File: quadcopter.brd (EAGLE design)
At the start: 127.2 x 127.2 mm, 77 parts, among them J1 AVR_SPI_PRG_6NS, J3 HEADER-0.1IN-2POS-FEMALE, J4 HEADER-0.1IN-2POS-FEMALE, J5 HEADER-0.1IN-2POS-FEMALE, J6 HEADER-0.1IN-2POS-FEMALE, J8 HEADER-0.1IN-2POS-FEMALE, SW1 PUSHBUTTON_SMD-VERTICAL, SW2 PUSHBUTTON_SMD-VERTICAL, U1 ATMEGA128RFA1

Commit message: fixed attenna
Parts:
- moved C2 0.13 mm to (-3.62, 23.8)
- moved C1 0.13 mm to (-3.37, 21.5)
- moved U$1 0.13 mm to (0.00, 29.7)
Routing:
- net GND: track 257.7 -> 246.4 mm, vias 8 -> 7

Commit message: changed caps, moving grounds
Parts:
- C18, C19, C20, C21: value 1uF -> 0.1uF
- moved C16 1.23 mm to (-24.1, -6.62), turned to 90 degrees
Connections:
- net BAT_GND: now also C16.2
- net GND: no longer C16.2
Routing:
- net GND: track 246.4 -> 251.7 mm
- net BAT_GND: track 143.7 -> 147.5 mm, vias 0 -> 1
- net V_BAT: track 85.6 -> 82.0 mm

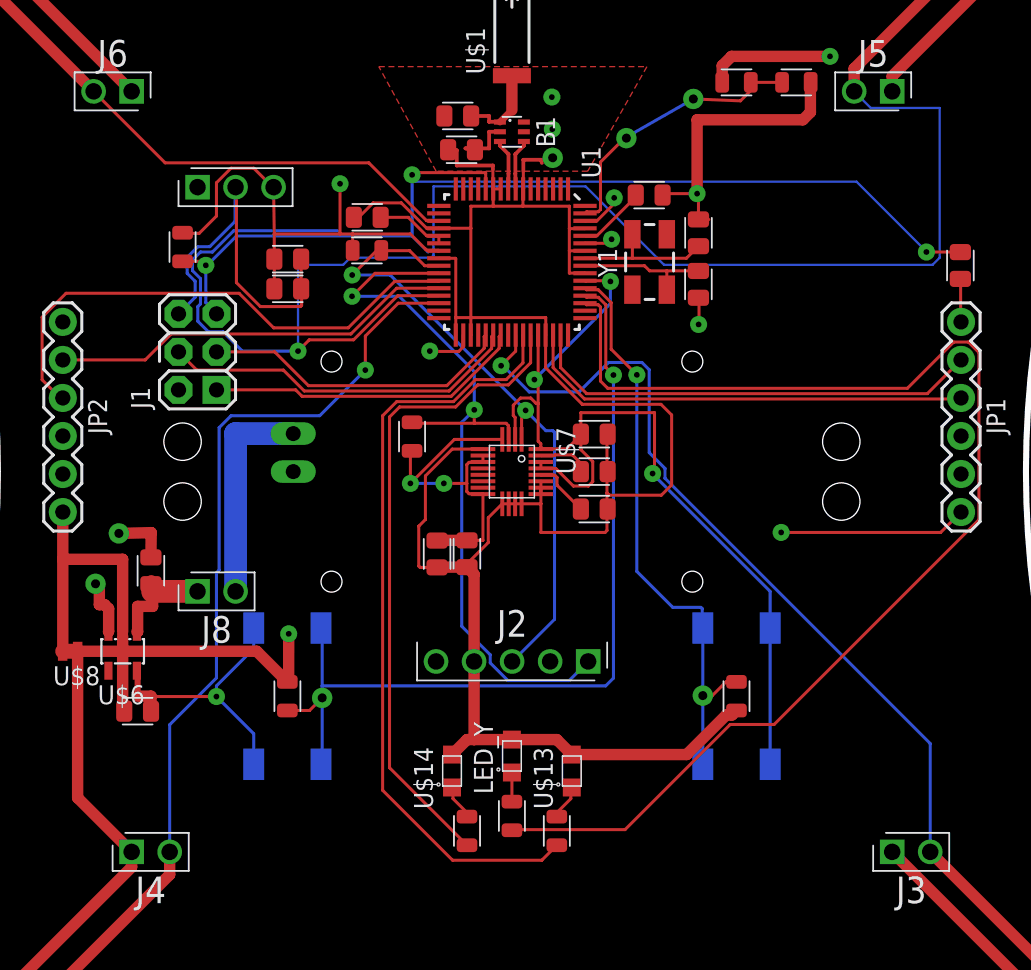
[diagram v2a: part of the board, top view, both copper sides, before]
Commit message: remapped and rewired M2_CTL and M3_CTL since the pins they were on were not originally PWM pins
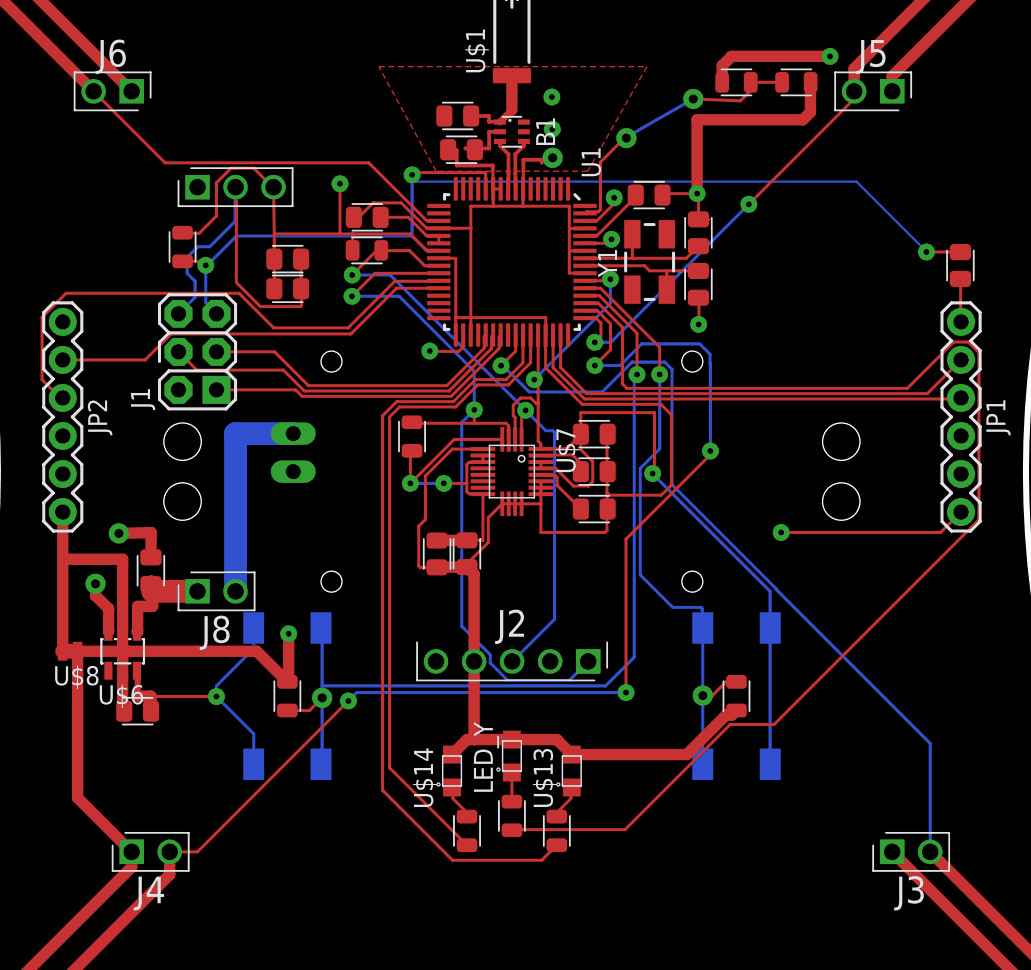
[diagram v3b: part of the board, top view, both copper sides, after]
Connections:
- net M2_CTL: now also U1.50; no longer U1.30
- net M3_CTL: now also U1.49; no longer U1.29
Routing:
- net M3_CTL: track 126.6 -> 48.8 mm, vias 1 -> 2
- net M2_CTL: track 70.4 -> 95.3 mm, vias 1 -> 4
- net BTN1: track 59.0 -> 60.4 mm
- net V_BAT: track 82.0 -> 80.7 mm
- net BTN2: track 39.3 -> 40.5 mm
- net M1_CTL: track 71.7 -> 72.6 mm
- net N$17: track 84.1 -> 83.4 mm

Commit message: dunno what i just did
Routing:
- net RESET: track 70.1 -> 68.6 mm
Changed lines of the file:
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@@
 <wire x1="-19.7358" y1="10.5791" x2="-19.73" y2="10.54" width="0.2032" layer="16"/>
 <wire x1="27.686" y1="14.6685" x2="29.8704" y2="14.6685" width="0.2032" layer="1"/>
-<wire x1="-6.6675" y1="15.7353" x2="-5.6007" y2="14.6685" width="0.2032" layer="16"/>
 <wire x1="-18.4023" y1="15.7353" x2="-6.6675" y2="15.7353" width="0.2032" layer="16"/>
 <wire x1="-20.3581" y1="13.7795" x2="-18.4023" y2="15.7353" width="0.2032" layer="16"/>

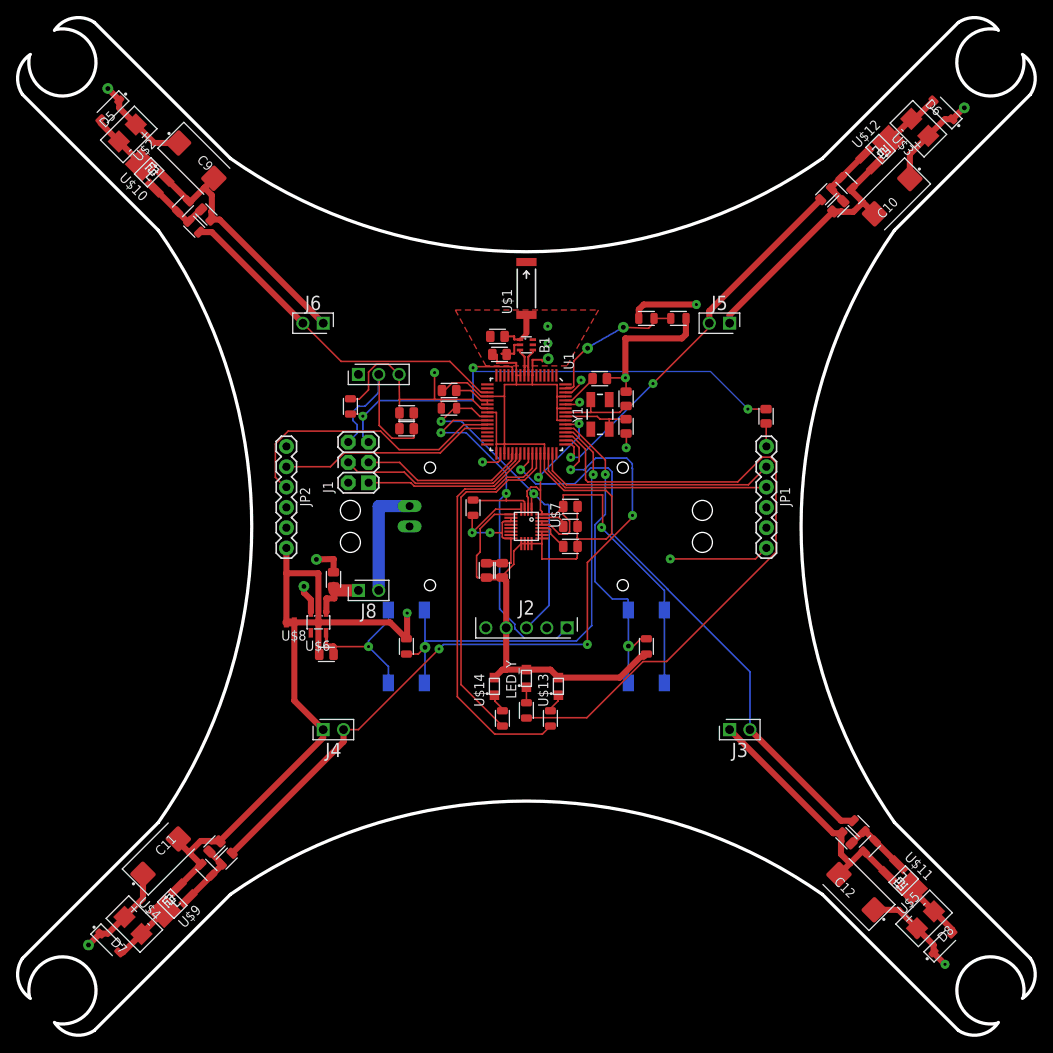
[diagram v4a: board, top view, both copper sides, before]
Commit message: added updated flybacks to board
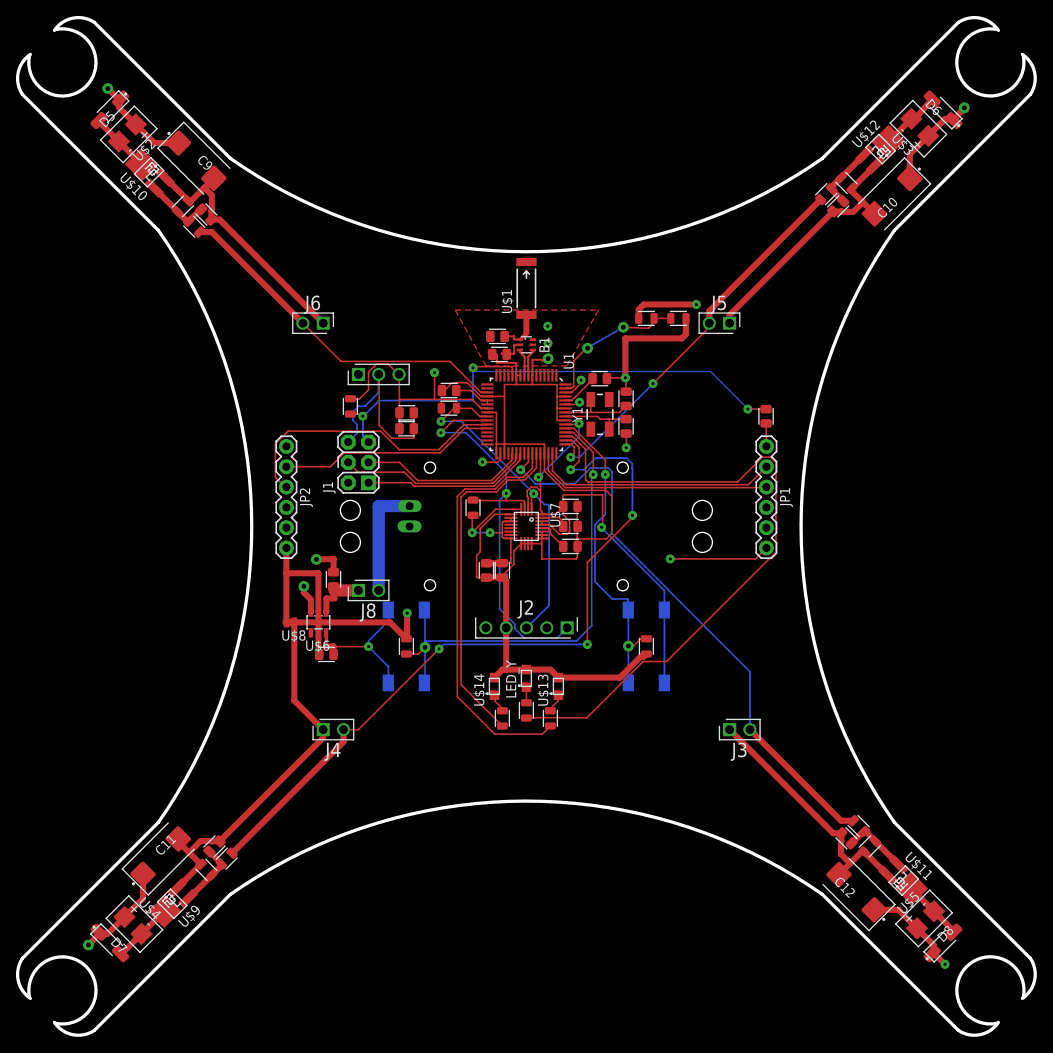
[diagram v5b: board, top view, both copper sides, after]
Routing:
- net V_BAT: track 80.7 -> 82.3 mm
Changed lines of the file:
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@@
 <?xml version="1.0" encoding="utf-8"?>
 <!DOCTYPE eagle SYSTEM "eagle.dtd">
-<eagle version="8.1.1">
+<eagle version="7.6.0">
 <drawing>
 <settings>
@@
 <wire x1="-25" y1="-9" x2="-24" y2="-9" width="0.762" layer="1"/>
 <via x="-54.737" y="-52.324" extent="1-16" drill="0.6"/>
-<wire x1="-53.213" y1="-50.927" x2="-53.24733125" y2="-50.892665625" width="0.762" layer="1"/>
+<wire x1="-53.213" y1="-50.927" x2="-53.4135" y2="-50.726496875" width="0.762" layer="1"/>
 <via x="54.737" y="52.324" extent="1-16" drill="0.6"/>
 <via x="-52.324" y="54.737" extent="1-16" drill="0.6"/>
@@
 <via x="21.2471" y="27.7368" extent="1-16" drill="0.381"/>
 <wire x1="-50.23710625" y1="-48.822890625" x2="-52.30688125" y2="-50.892665625" width="0.762" layer="1"/>
-<wire x1="-52.30688125" y1="-50.892665625" x2="-53.24733125" y2="-50.892665625" width="0.762" layer="1"/>
-<wire x1="-53.254865625" y1="-50.892665625" x2="-53.24733125" y2="-50.892665625" width="0.762" layer="1"/>
+<wire x1="-52.30688125" y1="-50.892665625" x2="-53.4135" y2="-50.726496875" width="0.762" layer="1"/>
+<wire x1="-53.254865625" y1="-50.892665625" x2="-53.4135" y2="-50.726496875" width="0.762" layer="1"/>
 <wire x1="48.822890625" y1="-51.17755625" x2="48.822890625" y2="-50.23710625" width="0.762" layer="1"/>
 <via x="52.324" y="-54.737" extent="1-16" drill="0.381"/>
@@
 <wire x1="46.51195625" y1="-47.926171875" x2="48.822890625" y2="-50.23710625" width="0.762" layer="1"/>
 <wire x1="48.822890625" y1="-50.23710625" x2="50.892665625" y2="-52.30688125" width="0.762" layer="1"/>
-<wire x1="50.892665625" y1="-52.30688125" x2="50.892665625" y2="-53.24733125" width="0.762" layer="1"/>
-<wire x1="-53.24733125" y1="-50.892665625" x2="-53.305665625" y2="-50.892665625" width="0.762" layer="1"/>
+<wire x1="50.892665625" y1="-52.30688125" x2="50.726496875" y2="-53.4135" width="0.762" layer="1"/>
+<wire x1="-53.4135" y1="-50.726496875" x2="-53.305665625" y2="-50.892665625" width="0.762" layer="1"/>
 <wire x1="-53.305665625" y1="-50.892665625" x2="-54.737" y2="-52.324" width="0.762" layer="1"/>
-<wire x1="50.892665625" y1="-53.24733125" x2="50.892665625" y2="-53.305665625" width="0.762" layer="1"/>
+<wire x1="50.726496875" y1="-53.4135" x2="50.892665625" y2="-53.305665625" width="0.762" layer="1"/>
 <wire x1="50.892665625" y1="-53.305665625" x2="52.324" y2="-54.737" width="0.762" layer="1"/>
 <wire x1="47.926171875" y1="43.481171875" x2="47.926171875" y2="46.51195625" width="0.762" layer="1"/>
 <wire x1="47.926171875" y1="46.51195625" x2="50.23710625" y2="48.822890625" width="0.762" layer="1"/>
 <wire x1="50.23710625" y1="48.822890625" x2="52.30688125" y2="50.892665625" width="0.762" layer="1"/>
-<wire x1="52.30688125" y1="50.892665625" x2="53.24733125" y2="50.892665625" width="0.762" layer="1"/>
-<wire x1="53.24733125" y1="50.892665625" x2="54.678665625" y2="52.324" width="0.762" layer="1"/>
+<wire x1="52.30688125" y1="50.892665625" x2="53.4135" y2="50.726496875" width="0.762" layer="1"/>
+<wire x1="53.4135" y1="50.726496875" x2="54.678665625" y2="52.324" width="0.762" layer="1"/>
 <wire x1="54.678665625" y1="52.324" x2="54.737" y2="52.324" width="0.762" layer="1"/>
 <wire x1="-43.481171875" y1="47.926171875" x2="-46.51195625" y2="47.926171875" width="0.762" layer="1"/>
 <wire x1="-46.51195625" y1="47.926171875" x2="-48.822890625" y2="50.23710625" width="0.762" layer="1"/>
 <wire x1="-48.822890625" y1="50.23710625" x2="-50.892665625" y2="52.30688125" width="0.762" layer="1"/>
-<wire x1="-50.892665625" y1="53.24733125" x2="-50.892665625" y2="52.30688125" width="0.762" layer="1"/>
+<wire x1="-50.726496875" y1="53.4135" x2="-50.892665625" y2="52.30688125" width="0.762" layer="1"/>
 <wire x1="-52.324" y1="54.737" x2="-50.892665625" y2="53.305665625" width="0.762" layer="1"/>
-<wire x1="-50.892665625" y1="53.305665625" x2="-50.892665625" y2="53.24733125" width="0.762" layer="1"/>
+<wire x1="-50.892665625" y1="53.305665625" x2="-50.726496875" y2="53.4135" width="0.762" layer="1"/>
 <wire x1="-21" y1="19" x2="-23.0378" y2="19" width="0.762" layer="2"/>
 <wire x1="-23.0378" y1="19" x2="-23.0378" y2="18.9992" width="0.762" layer="2"/>
@@
 <contactref element="D8" pad="A"/>
 <contactref element="U$11" pad="D"/>
-<wire x1="53.24733125" y1="-50.892665625" x2="53.24733125" y2="-50.418903125" width="0.762" layer="1"/>
+<wire x1="53.4135" y1="-50.726496875" x2="53.24733125" y2="-50.418903125" width="0.762" layer="1"/>
 <wire x1="50.9442125" y1="-48.115784375" x2="53.24733125" y2="-50.418903125" width="0.762" layer="1"/>
 <wire x1="48.118540625" y1="-45.2249875" x2="48.118540625" y2="-45.2901125" width="0.762" layer="1"/>
@@
 <wire x1="-48.118540625" y1="45.2901125" x2="-50.9442125" y2="48.115784375" width="0.762" layer="1"/>
 <wire x1="-50.9442125" y1="48.115784375" x2="-53.24733125" y2="50.418903125" width="0.762" layer="1"/>
-<wire x1="-53.24733125" y1="50.418903125" x2="-53.24733125" y2="50.892665625" width="0.2032" layer="1"/>
+<wire x1="-53.24733125" y1="50.418903125" x2="-53.4135" y2="50.726496875" width="0.2032" layer="1"/>
 </signal>
 <signal name="FLYBACK2" class="1">
@@
 <wire x1="45.2901125" y1="48.118540625" x2="48.115784375" y2="50.9442125" width="0.762" layer="1"/>
 <wire x1="48.115784375" y1="50.9442125" x2="48.589546875" y2="50.9442125" width="0.762" layer="1"/>
-<wire x1="48.589546875" y1="50.9442125" x2="50.892665625" y2="53.24733125" width="0.762" layer="1"/>
+<wire x1="48.589546875" y1="50.9442125" x2="50.726496875" y2="53.4135" width="0.762" layer="1"/>
 </signal>
 <signal name="FLYBACK3" class="1">
@@
 <wire x1="-45.2901125" y1="-48.118540625" x2="-45.2249875" y2="-48.118540625" width="0.762" layer="1"/>
 <wire x1="-48.115784375" y1="-50.9442125" x2="-50.418903125" y2="-53.24733125" width="0.762" layer="1"/>
-<wire x1="-50.418903125" y1="-53.24733125" x2="-50.892665625" y2="-53.24733125" width="0.762" layer="1"/>
+<wire x1="-50.418903125" y1="-53.24733125" x2="-50.726496875" y2="-53.4135" width="0.762" layer="1"/>
 </signal>
 <signal name="BTN1">

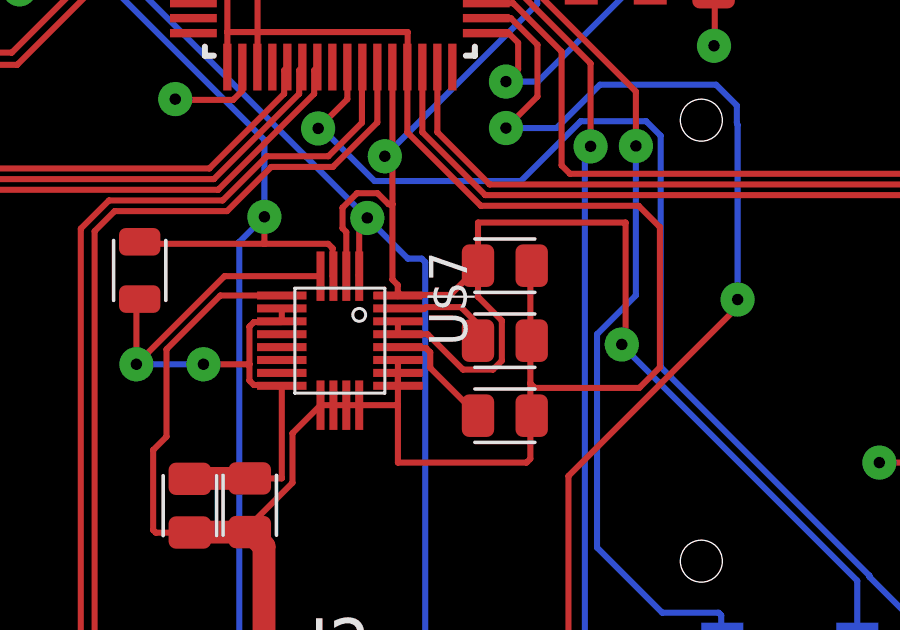
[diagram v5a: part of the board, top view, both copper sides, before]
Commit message: renaming parts
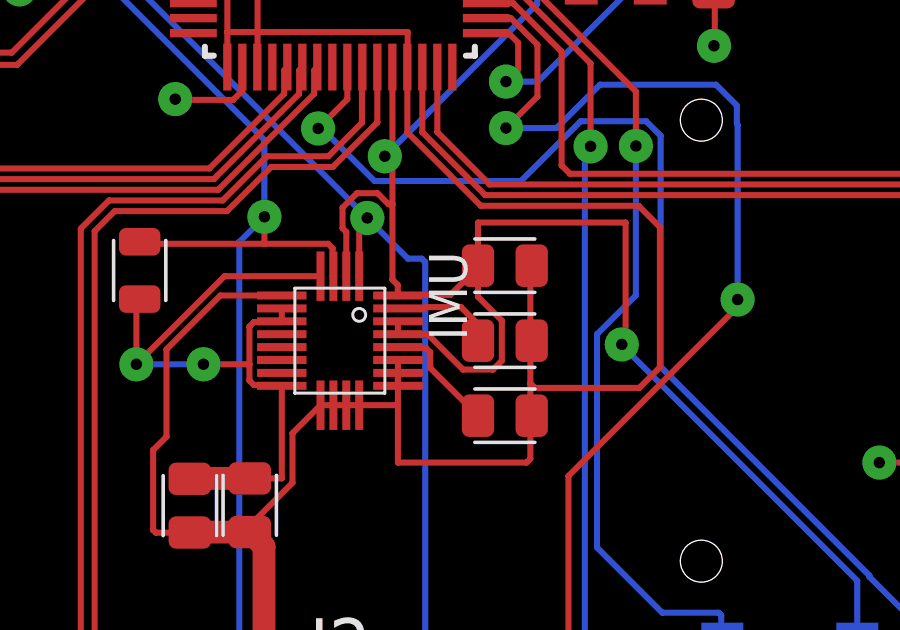
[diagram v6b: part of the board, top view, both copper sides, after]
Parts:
- renumbered U$7 to IMU
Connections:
- net V_BAT renamed VBAT
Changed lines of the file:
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@@
 <attribute name="PRICE" value="0.59" x="-26" y="-12" size="1.778" layer="27" rot="R180" display="off"/>
 </element>
-<element name="U$7" library="quadparts_michael" package="IMU_LSM9DS1TR" value="IMU" x="0" y="0" rot="R270">
+<element name="IMU" library="quadparts_michael" package="IMU_LSM9DS1TR" value="IMU" x="0" y="0" rot="R270">
 <attribute name="CREATOR" value="Michael M. Gonzalez" x="0" y="0" size="1.778" layer="27" rot="R270" display="off"/>
 <attribute name="DIST" value="Digikey" x="0" y="0" size="1.778" layer="27" rot="R270" display="off"/>
@@
 <contactref element="BATT1" pad="-"/>
 <contactref element="U$8" pad="P$2"/>
-<contactref element="U$7" pad="14"/>
-<contactref element="U$7" pad="15"/>
-<contactref element="U$7" pad="16"/>
-<contactref element="U$7" pad="17"/>
-<contactref element="U$7" pad="18"/>
-<contactref element="U$7" pad="19"/>
-<contactref element="U$7" pad="20"/>
+<contactref element="IMU" pad="14"/>
+<contactref element="IMU" pad="15"/>
+<contactref element="IMU" pad="16"/>
+<contactref element="IMU" pad="17"/>
+<contactref element="IMU" pad="18"/>
+<contactref element="IMU" pad="19"/>
+<contactref element="IMU" pad="20"/>
 <contactref element="R13" pad="1"/>
 <contactref element="JP1" pad="GND"/>
@@
 <contactref element="C13" pad="1"/>
 <contactref element="C14" pad="2"/>
-<contactref element="U$7" pad="6"/>
+<contactref element="IMU" pad="6"/>
 <contactref element="R15" pad="2"/>
 <contactref element="R16" pad="2"/>
@@
 <contactref element="U$6" pad="5"/>
 <contactref element="C17" pad="2"/>
-<contactref element="U$7" pad="22"/>
-<contactref element="U$7" pad="23"/>
-<contactref element="U$7" pad="1"/>
-<contactref element="U$7" pad="3"/>
+<contactref element="IMU" pad="22"/>
+<contactref element="IMU" pad="23"/>
+<contactref element="IMU" pad="1"/>
+<contactref element="IMU" pad="3"/>
 <contactref element="C6" pad="1"/>
 <contactref element="C7" pad="1"/>
@@
 <contactref element="J7" pad="3"/>
 <contactref element="J2" pad="5"/>
-<contactref element="U$7" pad="5"/>
-<contactref element="U$7" pad="7"/>
-<contactref element="U$7" pad="8"/>
-<contactref element="U$7" pad="13"/>
+<contactref element="IMU" pad="5"/>
+<contactref element="IMU" pad="7"/>
+<contactref element="IMU" pad="8"/>
+<contactref element="IMU" pad="13"/>
 <contactref element="R14" pad="1"/>
 <contactref element="R18" pad="1"/>
@@
 <via x="-26.254" y="-4.127" extent="1-16" drill="0.6"/>
 </signal>
-<signal name="V_BAT" class="1">
+<signal name="VBAT" class="1">
 <contactref element="U$3" pad="V+"/>
 <contactref element="C10" pad="1"/>
@@
 <signal name="SCL">
 <contactref element="U1" pad="25"/>
-<contactref element="U$7" pad="2"/>
+<contactref element="IMU" pad="2"/>
 <contactref element="J2" pad="3"/>
 <contactref element="R14" pad="2"/>
@@
 <signal name="SDA">
 <contactref element="U1" pad="26"/>
-<contactref element="U$7" pad="4"/>
+<contactref element="IMU" pad="4"/>
 <contactref element="J2" pad="1"/>
 <contactref element="R18" pad="2"/>
@@
 <signal name="N$9">
 <contactref element="C8" pad="1"/>
-<contactref element="U$7" pad="24"/>
+<contactref element="IMU" pad="24"/>
 <wire x1="2.8194" y1="1.0668" x2="1.9558" y2="1.0668" width="0.2032" layer="1"/>
 <wire x1="2.8702" y1="1.1176" x2="2.8194" y2="1.0668" width="0.2032" layer="1"/>
@@
 </signal>
 <signal name="N$14">
-<contactref element="U$7" pad="21"/>
+<contactref element="IMU" pad="21"/>
 <contactref element="C14" pad="1"/>
 <wire x1="1.935" y1="-0.215" x2="1.961" y2="-0.241" width="0.2032" layer="1"/>
